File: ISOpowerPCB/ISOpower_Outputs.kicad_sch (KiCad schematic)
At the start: 20 parts

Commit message: messing around with libraries
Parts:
- gave numbers to parts that had none: 20

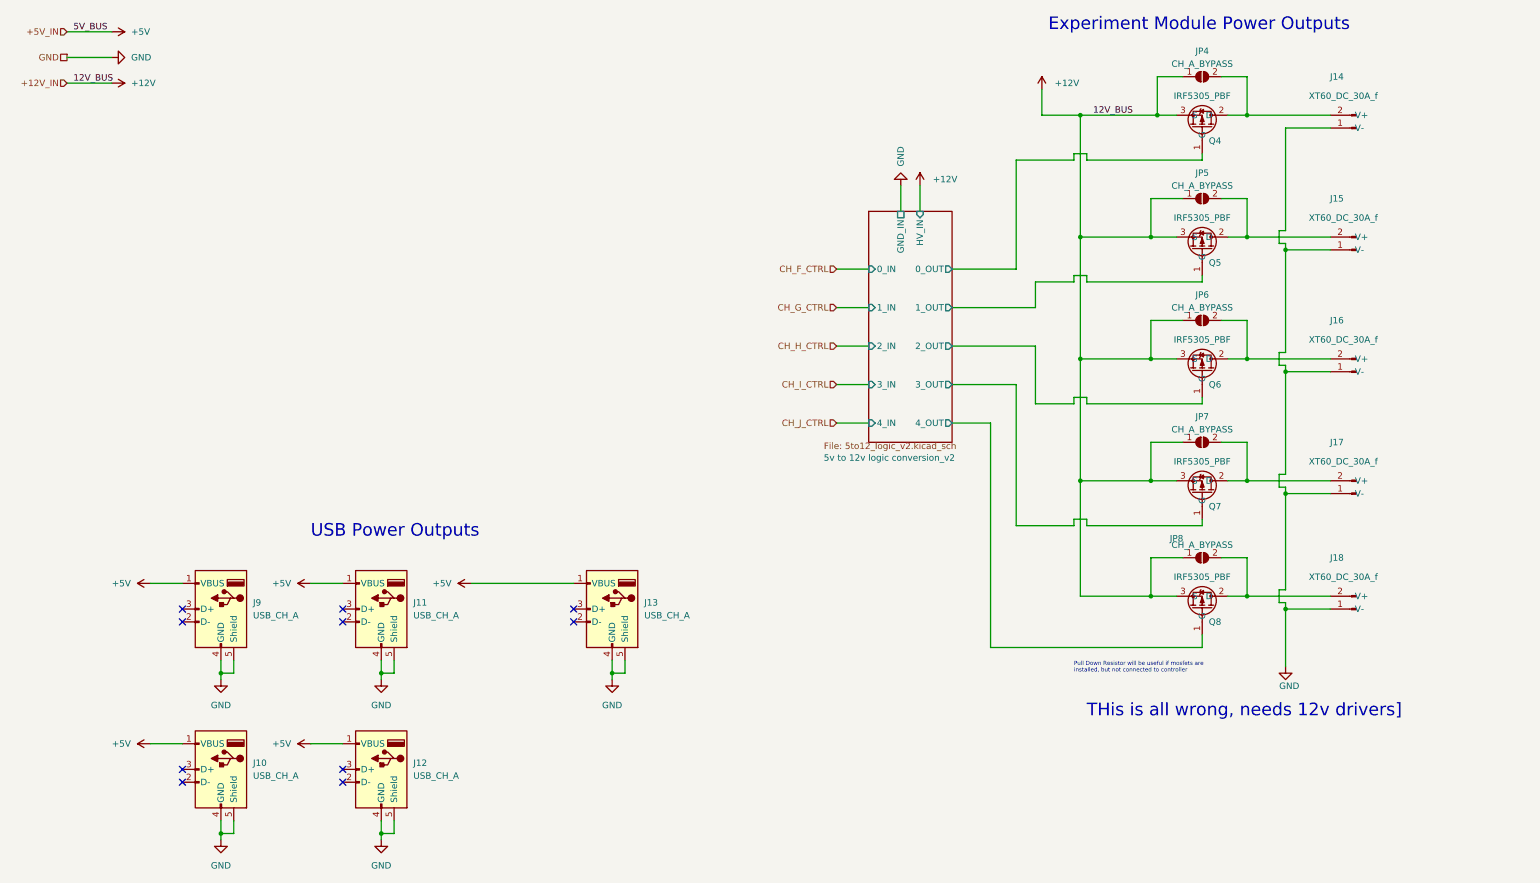
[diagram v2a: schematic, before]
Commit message: added documentation for component selection
Completed footprint association & added documentation re Netclasses. Need to update netclasses in schematic settings before moving to PCB layout.
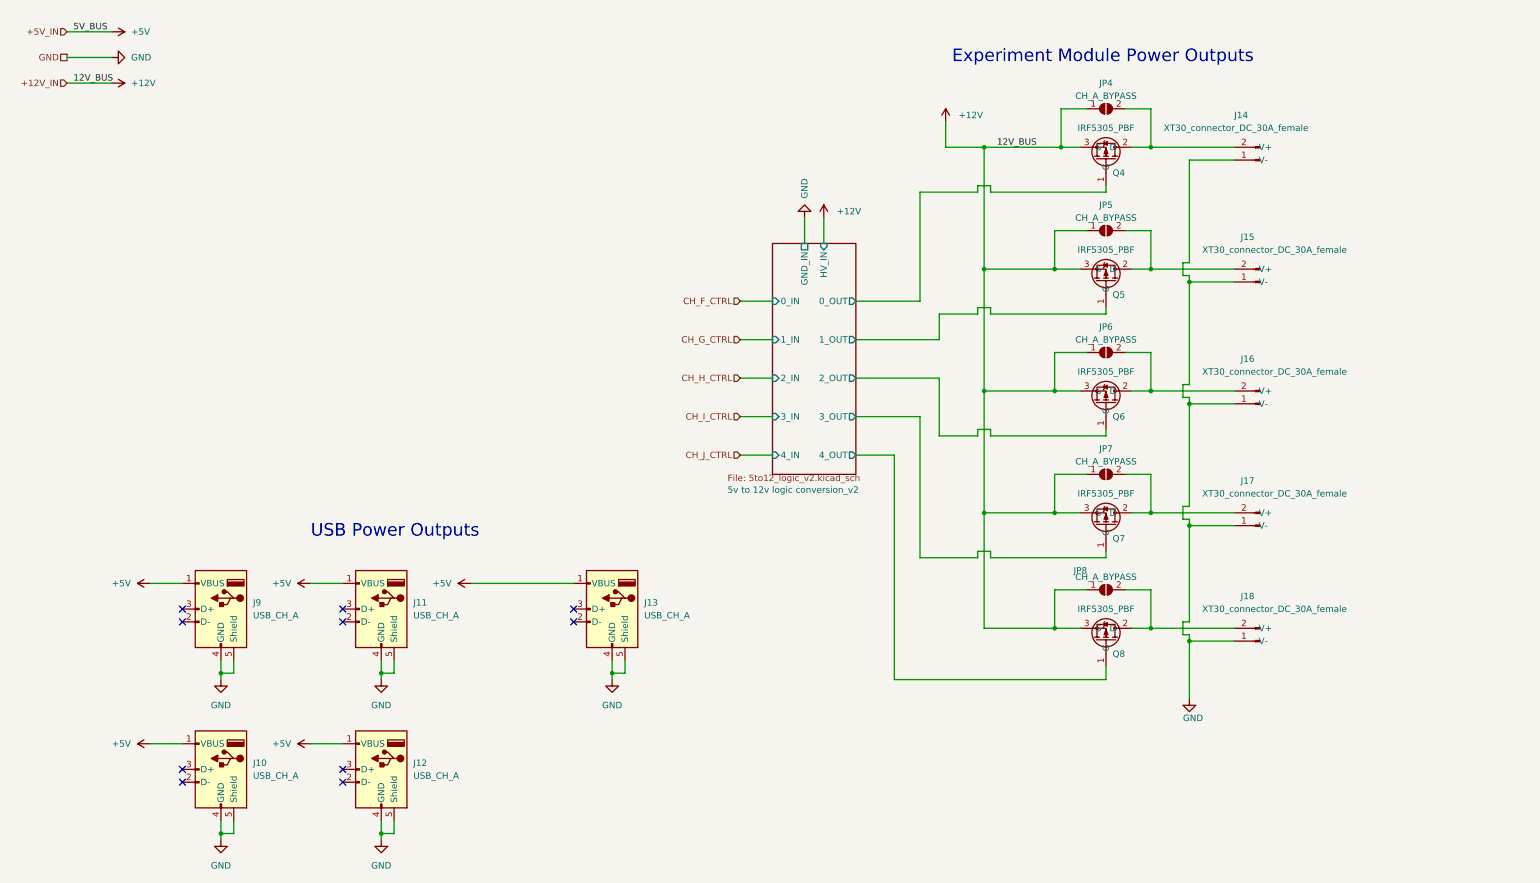
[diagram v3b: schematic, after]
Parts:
- removed J14, J15, J16, J17, J18: XT60_DC_30A_f, symbol 000_Connectors_Immo:XT60_connector_DC_30A_female
- added J14, J15, J16, J17, J18: XT30_connector_DC_30A_female, Connector_AMASS:AMASS_XT30PW-F_1x02_P2.50mm_Horizontal, symbol 000_Connectors_Immo:XT30_connector_DC_30A_female
- J10, J11, J12, J13, J9: footprint (none) -> Connector_USB:USB_A_Molex_67643_Horizontal
- JP4, JP5, JP6, JP7, JP8: footprint (none) -> Jumper:SolderJumper-2_P1.3mm_Open_RoundedPad1.0x1.5mm
- Q4, Q5, Q6, Q7, Q8: footprint Package_TO_SOT_THT:TO-220-3_Vertical -> Package_TO_SOT_SMD:TO-263-2
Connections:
- net GND: now also J14.1 (V-), J15.1 (V-), J16.1 (V-), J17.1 (V-), J18.1 (V-)
- net at JP6.2 (B), Q6.2 (D): now also J16.2 (V+)
- net at JP5.2 (B), Q5.2 (D): now also J15.2 (V+)
- net at JP4.2 (B), Q4.2 (D): now also J14.2 (V+)
- net at JP8.2 (B), Q8.2 (D): now also J18.2 (V+)
- net at JP7.2 (B), Q7.2 (D): now also J17.2 (V+)
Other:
- note removed: "Pull Down Resistor will be useful if mosfets are installed, but not connected to controller"
- note removed: "THis is all wrong, needs 12v drivers]"
- moved on the sheet: JP4, JP5, JP6, JP7, JP8, Q4, Q5, Q6, Q7, Q8

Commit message: added netclasses
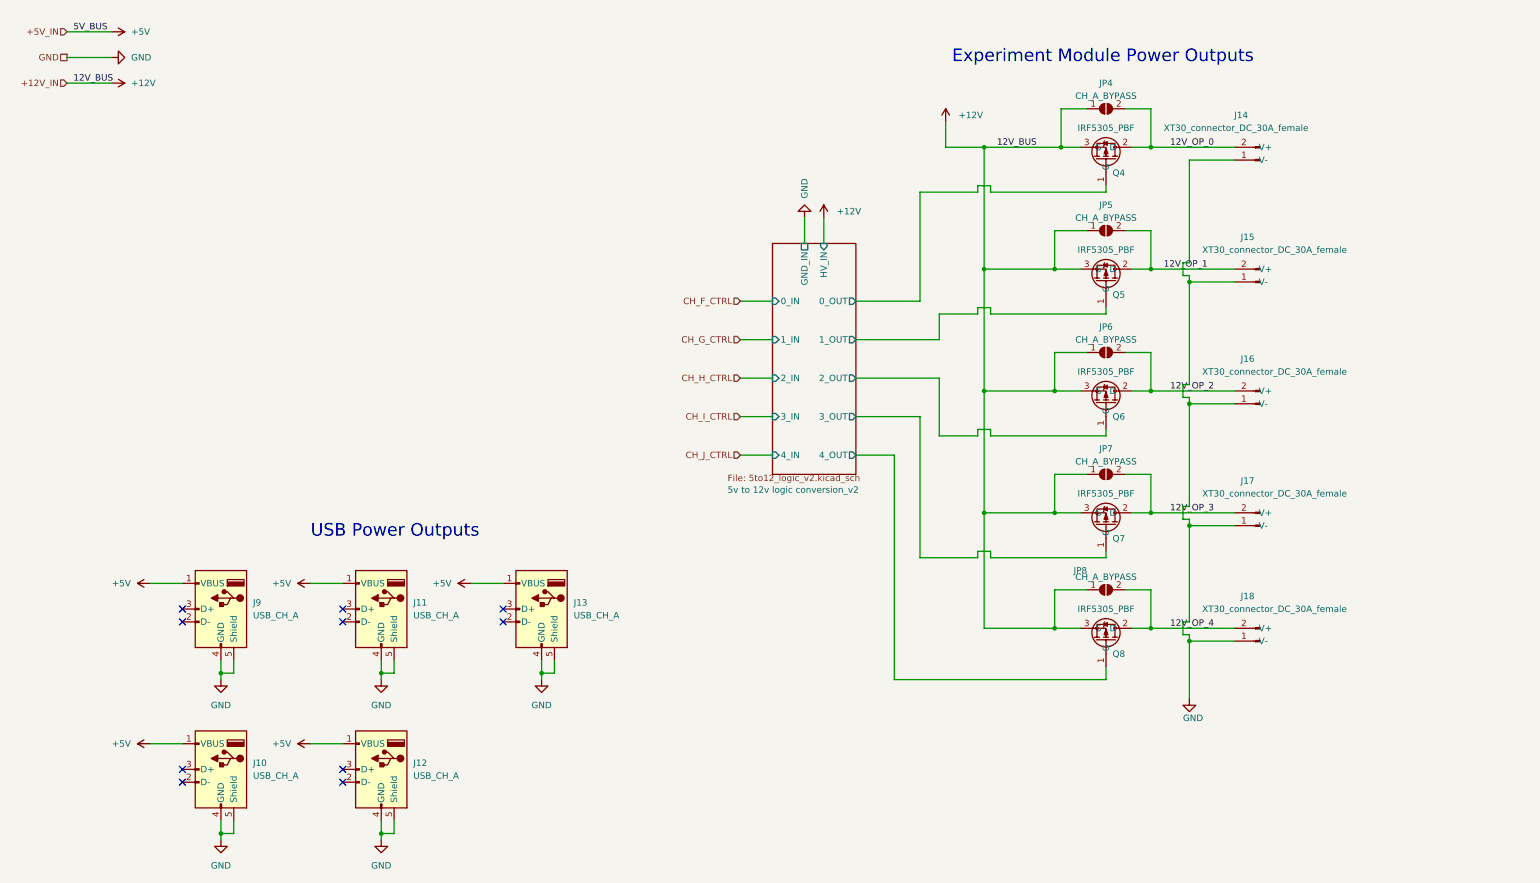
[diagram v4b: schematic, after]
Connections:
- net 12V_OP_2: now reaches J16.2 (V+), JP6.2 (B), Q6.2 (D)
- net 12V_OP_1: now reaches J15.2 (V+), JP5.2 (B), Q5.2 (D)
- net 12V_OP_4: now reaches J18.2 (V+), JP8.2 (B), Q8.2 (D)
- net 12V_OP_3: now reaches J17.2 (V+), JP7.2 (B), Q7.2 (D)
- net 12V_OP_0: now reaches J14.2 (V+), JP4.2 (B), Q4.2 (D)
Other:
- moved on the sheet: J13
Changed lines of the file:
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@@
   (junction (at 204.47 114.3) (diameter 0) (color 0 0 0 0)
   )
-  (junction (at 130.81 146.05) (diameter 0) (color 0 0 0 0)
+  (junction (at 116.84 146.05) (diameter 0) (color 0 0 0 0)
   )
   (junction (at 204.47 41.91) (diameter 0) (color 0 0 0 0)
@@
   (no_connect (at 45.72 165.1))
   (no_connect (at 77.47 133.35))
-  (no_connect (at 123.19 135.89))
-  (no_connect (at 123.19 133.35))
+  (no_connect (at 109.22 135.89))
+  (no_connect (at 109.22 133.35))
   (no_connect (at 77.47 165.1))
   (no_connect (at 77.47 167.64))
@@
     (stroke (width 0) (type default) (color 0 0 0 0))
   )
-  (wire (pts (xy 130.81 146.05) (xy 130.81 147.32))
+  (wire (pts (xy 116.84 146.05) (xy 116.84 147.32))
     (stroke (width 0) (type default) (color 0 0 0 0))
   )
@@
     (stroke (width 0) (type default) (color 0 0 0 0))
   )
-  (wire (pts (xy 130.81 146.05) (xy 133.35 146.05))
+  (wire (pts (xy 116.84 146.05) (xy 119.38 146.05))
     (stroke (width 0) (type default) (color 0 0 0 0))
   )
@@
     (stroke (width 0) (type default) (color 0 0 0 0))
   )
-  (wire (pts (xy 133.35 146.05) (xy 133.35 143.51))
+  (wire (pts (xy 119.38 146.05) (xy 119.38 143.51))
     (stroke (width 0) (type default) (color 0 0 0 0))
   )
@@
     (stroke (width 0) (type default) (color 0 0 0 0))
   )
-  (wire (pts (xy 102.87 128.27) (xy 123.19 128.27))
+  (wire (pts (xy 102.87 128.27) (xy 109.22 128.27))
     (stroke (width 0) (type default) (color 0 0 0 0))
   )
@@
     (stroke (width 0) (type default) (color 0 0 0 0))
   )
-  (wire (pts (xy 130.81 143.51) (xy 130.81 146.05))
+  (wire (pts (xy 116.84 143.51) (xy 116.84 146.05))
     (stroke (width 0) (type default) (color 0 0 0 0))
   )
@@
     (effects (font (size 2.5 2.5)) (justify left bottom))
   )
+  (label "12V_OP_0" (at 241.3 41.91 0)
+    (effects (font (size 1.27 1.27)) (justify left bottom))
+  )
+  (label "12V_OP_1" (at 240.03 66.04 0)
+    (effects (font (size 1.27 1.27)) (justify left bottom))
+  )
+  (label "12V_OP_2" (at 241.3 90.17 0)
+    (effects (font (size 1.27 1.27)) (justify left bottom))
+  )
+  (label "12V_OP_4" (at 241.3 137.16 0)
+    (effects (font (size 1.27 1.27)) (justify left bottom))
+  )
   (label "12V_BUS" (at 207.01 41.91 0)
+    (effects (font (size 1.27 1.27)) (justify left bottom))
+  )
+  (label "12V_OP_3" (at 241.3 114.3 0)
     (effects (font (size 1.27 1.27)) (justify left bottom))
   )
@@
     (pin "1")
   )
-  (symbol (lib_id "power:GND") (at 130.81 147.32 0) (unit 1)
-    (in_bom yes) (on_board yes) (fields_autoplaced)
-    (property "Reference" "#PWR064" (id 0) (at 130.81 153.67 0)
-      (effects (font (size 1.27 1.27)) hide)
-    )
-    (property "Value" "GND" (id 1) (at 130.81 152.4 0))
-    (property "Footprint" "" (id 2) (at 130.81 147.32 0)
-      (effects (font (size 1.27 1.27)) hide)
-    )
-    (property "Datasheet" "" (id 3) (at 130.81 147.32 0)
+  (symbol (lib_id "power:GND") (at 116.84 147.32 0) (unit 1)
+    (in_bom yes) (on_board yes) (fields_autoplaced)
+    (property "Reference" "#PWR064" (id 0) (at 116.84 153.67 0)
+      (effects (font (size 1.27 1.27)) hide)
+    )
+    (property "Value" "GND" (id 1) (at 116.84 152.4 0))
+    (property "Footprint" "" (id 2) (at 116.84 147.32 0)
+      (effects (font (size 1.27 1.27)) hide)
+    )
+    (property "Datasheet" "" (id 3) (at 116.84 147.32 0)
       (effects (font (size 1.27 1.27)) hide)
     )
@@
     (pin "1")
   )
-  (symbol (lib_id "Connector:USB_A") (at 130.81 133.35 0) (mirror y) (unit 1)
-    (in_bom yes) (on_board yes) (fields_autoplaced)
-    (property "Reference" "J13" (id 0) (at 137.16 132.0799 0)
-      (effects (font (size 1.27 1.27)) (justify right))
-    )
-    (property "Value" "USB_CH_A" (id 1) (at 137.16 134.6199 0)
-      (effects (font (size 1.27 1.27)) (justify right))
-    )
-    (property "Footprint" "Connector_USB:USB_A_Molex_67643_Horizontal" (id 2) (at 127 134.62 0)
-      (effects (font (size 1.27 1.27)) hide)
-    )
-    (property "Datasheet" " ~" (id 3) (at 127 134.62 0)
-      (effects (font (size 1.27 1.27)) hide)
-    )
+  (symbol (lib_id "Connector:USB_A") (at 116.84 133.35 0) (mirror y) (unit 1)
+    (in_bom yes) (on_board yes) (fields_autoplaced)
+    (property "Reference" "J13" (id 0) (at 123.19 132.0799 0)
+      (effects (font (size 1.27 1.27)) (justify right))
+    )
+    (property "Value" "USB_CH_A" (id 1) (at 123.19 134.6199 0)
+      (effects (font (size 1.27 1.27)) (justify right))
+    )
+    (property "Footprint" "Connector_USB:USB_A_Molex_67643_Horizontal" (id 2) (at 113.03 134.62 0)
+      (effects (font (size 1.27 1.27)) hide)
+    )
+    (property "Datasheet" " ~" (id 3) (at 113.03 134.62 0)
+      (effects (font (size 1.27 1.27)) hide)
+    )

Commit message: PCB Layouts
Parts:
- JP4: value CH_A_BYPASS -> OP_0
- JP5: value CH_A_BYPASS -> OP_1
- JP6: value CH_A_BYPASS -> OP_2
- JP7: value CH_A_BYPASS -> OP_3
- JP8: value CH_A_BYPASS -> OP_4
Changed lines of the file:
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@@
     (in_bom yes) (on_board yes)
     (property "Reference" "JP7" (id 0) (at 228.6 101.6 0))
-    (property "Value" "CH_A_BYPASS" (id 1) (at 228.6 104.14 0))
+    (property "Value" "OP_3" (id 1) (at 228.6 104.14 0))
     (property "Footprint" "Jumper:SolderJumper-2_P1.3mm_Open_RoundedPad1.0x1.5mm" (id 2) (at 228.6 106.68 0)
       (effects (font (size 1.27 1.27)) hide)
@@
     (in_bom yes) (on_board yes)
     (property "Reference" "JP6" (id 0) (at 228.6 77.47 0))
-    (property "Value" "CH_A_BYPASS" (id 1) (at 228.6 80.01 0))
+    (property "Value" "OP_2" (id 1) (at 228.6 80.01 0))
     (property "Footprint" "Jumper:SolderJumper-2_P1.3mm_Open_RoundedPad1.0x1.5mm" (id 2) (at 228.6 82.55 0)
       (effects (font (size 1.27 1.27)) hide)
@@
     (in_bom yes) (on_board yes)
     (property "Reference" "JP4" (id 0) (at 228.6 29.21 0))
-    (property "Value" "CH_A_BYPASS" (id 1) (at 228.6 31.75 0))
+    (property "Value" "OP_0" (id 1) (at 228.6 31.75 0))
     (property "Footprint" "Jumper:SolderJumper-2_P1.3mm_Open_RoundedPad1.0x1.5mm" (id 2) (at 228.6 34.29 0)
       (effects (font (size 1.27 1.27)) hide)
@@
     (in_bom yes) (on_board yes)
     (property "Reference" "JP8" (id 0) (at 223.52 125.73 0))
-    (property "Value" "CH_A_BYPASS" (id 1) (at 228.6 127 0))
+    (property "Value" "OP_4" (id 1) (at 228.6 127 0))
     (property "Footprint" "Jumper:SolderJumper-2_P1.3mm_Open_RoundedPad1.0x1.5mm" (id 2) (at 228.6 129.54 0)
       (effects (font (size 1.27 1.27)) hide)
@@
     (in_bom yes) (on_board yes)
     (property "Reference" "JP5" (id 0) (at 228.6 53.34 0))
-    (property "Value" "CH_A_BYPASS" (id 1) (at 228.6 55.88 0))
+    (property "Value" "OP_1" (id 1) (at 228.6 55.88 0))
     (property "Footprint" "Jumper:SolderJumper-2_P1.3mm_Open_RoundedPad1.0x1.5mm" (id 2) (at 228.6 58.42 0)
       (effects (font (size 1.27 1.27)) hide)
